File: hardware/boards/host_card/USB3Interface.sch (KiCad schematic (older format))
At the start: 8 parts, among them J2 USB3_Micro_B_Amphenol, J5 Conn_02x04_Odd_Even, U1 ECP5UM5G-381caBGA, U3 CYUSB3014, U6 128MiB

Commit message: Added a fiducial to for U7. Changed the two pin-headers to the keyd  samtec connectors. Some other misc updates
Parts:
- J5: footprint Connector_PinHeader_1.27mm:PinHeader_2x05_P1.27mm_Vertical -> lethalbit-connectors:FTSH-105-01-L-DV-K-TR
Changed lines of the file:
@@
 F 0 "J5" H 6400 7150 50  0000 C CNN
 F 1 "Conn_02x04_Odd_Even" H 6400 7250 50  0000 C CNN
-F 2 "Connector_PinHeader_1.27mm:PinHeader_2x05_P1.27mm_Vertical" H 6350 6800 50  0001 C CNN
+F 2 "lethalbit-connectors:FTSH-105-01-L-DV-K-TR" H 6350 6800 50  0001 C CNN
 F 3 "~" H 6350 6800 50  0001 C CNN
 	1    6350 6800

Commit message: Fixed up the consistancy of value naming, 100nF -> 0.1uF. Added the caps for the USB SSRX lines, moved the Ferrite for VBUS to fix a net naming issue
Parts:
- added C77, C78: 0.1uF, Capacitor_SMD:C_0402_1005Metric, symbol Device:C_Small
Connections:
- net SSTX+: now also C77.2; no longer U3.A5 (SSTX_P)
- net SSTX-: now also C78.2; no longer U3.A6 (SSTX_N)
- new net: C78.1, U3.A6 (SSTX_N)
- new net: C77.1, U3.A5 (SSTX_P)
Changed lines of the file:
@@
 	800  700  1050 700
 Wire Wire Line
-	2350 1800 3600 1800
-Wire Wire Line
 	3600 1800 3600 1550
 Wire Wire Line
 	3600 1550 3450 1550
 Wire Wire Line
-	2350 1900 3650 1900
-Wire Wire Line
 	3650 1900 3650 1650
 Wire Wire Line
 	3650 1650 3450 1650
 Wire Wire Line
-	2350 2050 3800 2050
+	2350 2050 3150 2050
 Wire Wire Line
 	3800 2050 3800 1250
@@
 	3800 1250 3450 1250
 Wire Wire Line
-	2350 2150 3850 2150
+	2350 2150 3050 2150
 Wire Wire Line
 	3850 2150 3850 1350
@@
 Text Notes 5900 3750 0    50   ~ 0
 PHY Boot config\n0 0 X - Sync ADMux\n1 0 X - Async ADMux\n1 1 X - USB\n1 X 0 - SPI, USB On failure
+Wire Wire Line
+	2350 1900 3650 1900
+Wire Wire Line
+	2350 1800 3600 1800
+$Comp
+L Device:C_Small C?
+U 1 1 5F3166F0
+P 3150 2150
+AR Path="/5EF66188/5F3166F0" Ref="C?"  Part="1"
+AR Path="/5ED4B101/5F3166F0" Ref="C?"  Part="1"
+AR Path="/5F2CAFD2/5F3166F0" Ref="C77"  Part="1"
+F 0 "C77" V 3200 1950 50  0000 L CNN
+F 1 "0.1uF" V 3350 2250 50  0000 L CNN
+F 2 "Capacitor_SMD:C_0402_1005Metric" H 3150 2150 50  0001 C CNN
+F 3 "~" H 3150 2150 50  0001 C CNN
+F 4 "KEMET" H 3150 2150 50  0001 C CNN "MFR"
+F 5 "C0402C104M8PACTU" H 3150 2150 50  0001 C CNN "MPN"
+	1    3150 2150
+	0    1    -1   0
+$EndComp
+$Comp
+L Device:C_Small C?
+U 1 1 5F3166E8
+P 3250 2050
+AR Path="/5EF66188/5F3166E8" Ref="C?"  Part="1"
+AR Path="/5ED4B101/5F3166E8" Ref="C?"  Part="1"
+AR Path="/5F2CAFD2/5F3166E8" Ref="C78"  Part="1"
+F 0 "C78" V 3300 1850 50  0000 L CNN
+F 1 "0.1uF" V 3350 2050 50  0000 L CNN
+F 2 "Capacitor_SMD:C_0402_1005Metric" H 3250 2050 50  0001 C CNN
+F 3 "~" H 3250 2050 50  0001 C CNN
+F 4 "KEMET" H 3250 2050 50  0001 C CNN "MFR"
+F 5 "C0402C104M8PACTU" H 3250 2050 50  0001 C CNN "MPN"
+	1    3250 2050
+	0    1    -1   0
+$EndComp
+Wire Wire Line
+	3250 2150 3850 2150
+Wire Wire Line
+	3350 2050 3800 2050
 Wire Bus Line
 	3150 3400 3150 4950

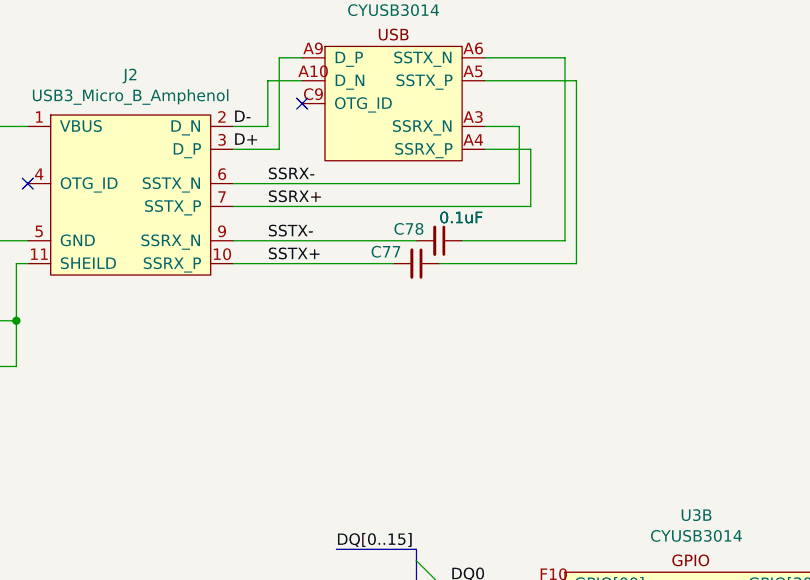
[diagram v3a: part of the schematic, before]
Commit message: Re-routed the USB side of things after adding the ESD diodes for the USB SS lines, still need to add the diode for the normal D+/D- pair
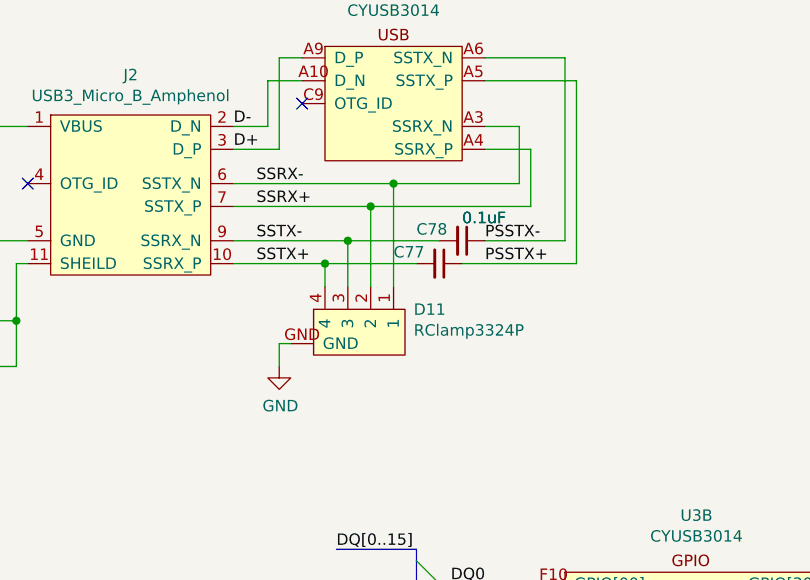
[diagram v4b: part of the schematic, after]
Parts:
- added D11: RClamp3324P, lethalbit:RClamp3324P, symbol lethalbit:RClamp3324P
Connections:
- net GND: now also D11.GND
- net SSRX+: now also D11.2
- net SSRX-: now also D11.1
- net SSTX+: now also D11.4
- net SSTX-: now also D11.3
- net PSSTX-: now reaches C78.1, U3.A6 (SSTX_N)
- net PSSTX+: now reaches C77.1, U3.A5 (SSTX_P)
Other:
- moved on the sheet: C77, C78
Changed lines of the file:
@@
 	3650 1650 3450 1650
 Wire Wire Line
-	2350 2050 3150 2050
+	2350 2050 2850 2050
 Wire Wire Line
 	3800 2050 3800 1250
@@
 	3800 1250 3450 1250
 Wire Wire Line
-	2350 2150 3050 2150
+	2350 2150 2750 2150
 Wire Wire Line
 	3850 2150 3850 1350
 Wire Wire Line
 	3850 1350 3450 1350
-Text Label 2500 1800 0    50   ~ 0
+Text Label 2450 1800 0    50   ~ 0
 SSRX-
-Text Label 2500 1900 0    50   ~ 0
+Text Label 2450 1900 0    50   ~ 0
 SSRX+
-Text Label 2500 2050 0    50   ~ 0
+Text Label 2450 2050 0    50   ~ 0
 SSTX-
-Text Label 2500 2150 0    50   ~ 0
+Text Label 2450 2150 0    50   ~ 0
 SSTX+
 Text Label 2350 1650 0    50   ~ 0
@@
 PHY Boot config\n0 0 X - Sync ADMux\n1 0 X - Async ADMux\n1 1 X - USB\n1 X 0 - SPI, USB On failure
 Wire Wire Line
-	2350 1900 3650 1900
-Wire Wire Line
-	2350 1800 3600 1800
+	2350 1900 2950 1900
+Wire Wire Line
+	2350 1800 3050 1800
 $Comp
 L Device:C_Small C?
 U 1 1 5F3166F0
-P 3150 2150
+P 3250 2150
 AR Path="/5EF66188/5F3166F0" Ref="C?"  Part="1"
 AR Path="/5ED4B101/5F3166F0" Ref="C?"  Part="1"
 AR Path="/5F2CAFD2/5F3166F0" Ref="C77"  Part="1"
-F 0 "C77" V 3200 1950 50  0000 L CNN
-F 1 "0.1uF" V 3350 2250 50  0000 L CNN
-F 2 "Capacitor_SMD:C_0402_1005Metric" H 3150 2150 50  0001 C CNN
-F 3 "~" H 3150 2150 50  0001 C CNN
-F 4 "KEMET" H 3150 2150 50  0001 C CNN "MFR"
-F 5 "C0402C104M8PACTU" H 3150 2150 50  0001 C CNN "MPN"
-	1    3150 2150
+F 0 "C77" V 3300 1950 50  0000 L CNN
+F 1 "0.1uF" V 3450 2250 50  0000 L CNN
+F 2 "Capacitor_SMD:C_0402_1005Metric" H 3250 2150 50  0001 C CNN
+F 3 "~" H 3250 2150 50  0001 C CNN
+F 4 "KEMET" H 3250 2150 50  0001 C CNN "MFR"
+F 5 "C0402C104M8PACTU" H 3250 2150 50  0001 C CNN "MPN"
+	1    3250 2150
 	0    1    -1   0
 $EndComp
@@
 L Device:C_Small C?
 U 1 1 5F3166E8
-P 3250 2050
+P 3350 2050
 AR Path="/5EF66188/5F3166E8" Ref="C?"  Part="1"
 AR Path="/5ED4B101/5F3166E8" Ref="C?"  Part="1"
 AR Path="/5F2CAFD2/5F3166E8" Ref="C78"  Part="1"
-F 0 "C78" V 3300 1850 50  0000 L CNN
-F 1 "0.1uF" V 3350 2050 50  0000 L CNN
-F 2 "Capacitor_SMD:C_0402_1005Metric" H 3250 2050 50  0001 C CNN
-F 3 "~" H 3250 2050 50  0001 C CNN
-F 4 "KEMET" H 3250 2050 50  0001 C CNN "MFR"
-F 5 "C0402C104M8PACTU" H 3250 2050 50  0001 C CNN "MPN"
-	1    3250 2050
+F 0 "C78" V 3400 1850 50  0000 L CNN
+F 1 "0.1uF" V 3450 2050 50  0000 L CNN
+F 2 "Capacitor_SMD:C_0402_1005Metric" H 3350 2050 50  0001 C CNN
+F 3 "~" H 3350 2050 50  0001 C CNN
+F 4 "KEMET" H 3350 2050 50  0001 C CNN "MFR"
+F 5 "C0402C104M8PACTU" H 3350 2050 50  0001 C CNN "MPN"
+	1    3350 2050
 	0    1    -1   0
 $EndComp
 Wire Wire Line
-	3250 2150 3850 2150
-Wire Wire Line
-	3350 2050 3800 2050
+	3350 2150 3850 2150
+Wire Wire Line
+	3450 2050 3800 2050
+Text Label 3450 2050 0    50   ~ 0
+PSSTX-
+Text Label 3450 2150 0    50   ~ 0
+PSSTX+
+$Comp
+L lethalbit:RClamp3324P D11
+U 1 1 5F4285A2
+P 2900 2500
+F 0 "D11" H 2662 2351 50  0000 R CNN
+F 1 "RClamp3324P" H 2662 2442 50  0000 R CNN
+F 2 "lethalbit:RClamp3324P" H 2900 2650 50  0001 C CNN
+F 3 "https://semtech.my.salesforce.com/sfc/p/#E0000000JelG/a/2R0000001NiZ/qbDz15IGGVdaTdo1LADFZxj6et0pDkRtmnKBn3k6s2M" H 2900 2650 50  0001 C CNN
+F 4 "Semtech Corporation" H 2900 2500 50  0001 C CNN "MFR"
+F 5 "RCLAMP3324P.TNT" H 2900 2500 50  0001 C CNN "MPN"
+	1    2900 2500
+	-1   0    0    1
+$EndComp
+Wire Wire Line
+	3050 2250 3050 1800
+Connection ~ 3050 1800
+Wire Wire Line
+	3050 1800 3600 1800
+Wire Wire Line
+	2950 2250 2950 1900
+Connection ~ 2950 1900
+Wire Wire Line
+	2950 1900 3650 1900
+Wire Wire Line
+	2850 2250 2850 2050
+Connection ~ 2850 2050
+Wire Wire Line
+	2850 2050 3250 2050
+Wire Wire Line
+	2750 2250 2750 2150
+Connection ~ 2750 2150
+Wire Wire Line
+	2750 2150 3150 2150
+$Comp
+L power:GND #PWR0144
+U 1 1 5F45C5E7
+P 2550 2600
+F 0 "#PWR0144" H 2550 2350 50  0001 C CNN
+F 1 "GND" H 2555 2427 50  0000 C CNN
+F 2 "" H 2550 2600 50  0001 C CNN
+F 3 "" H 2550 2600 50  0001 C CNN
+	1    2550 2600
+	1    0    0    -1
+$EndComp
+Wire Wire Line
+	2600 2500 2550 2500
+Wire Wire Line
+	2550 2500 2550 2600
 Wire Bus Line
 	3150 3400 3150 4950

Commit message: Roughly grouped unplaced parts together based on what they are related to
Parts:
- added D12: RClamp0512, lethalbit:RClamp0512, symbol lethalbit:RClamp0512
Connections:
- net D+: now also D12.2
- net D-: now also D12.1
- net GND: now also D12.GND
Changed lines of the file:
@@
 	2350 1550 2500 1550
 Wire Wire Line
-	2500 1550 2500 1350
+	2500 1550 2500 1400
 Wire Wire Line
 	2500 1350 2650 1350
@@
 Wire Wire Line
 	2550 2500 2550 2600
+$Comp
+L lethalbit:RClamp0512 D12
+U 1 1 5FB167E7
+P 2450 850
+F 0 "D12" H 2508 1125 50  0000 C CNN
+F 1 "RClamp0512" H 2508 1034 50  0000 C CNN
+F 2 "lethalbit:RClamp0512" H 2450 1000 50  0001 C CNN
+F 3 "https://media.digikey.com/pdf/Data%20Sheets/Semtech%20PDFs/RCLAMP0512TQ_Rev6_12-17-15.pdf" H 2450 1000 50  0001 C CNN
+F 4 "Sametech" H 2450 850 50  0001 C CNN "MFR"
+F 5 "RCLAMP0512TQTCT" H 2450 850 50  0001 C CNN "MPN"
+	1    2450 850
+	1    0    0    -1
+$EndComp
+Wire Wire Line
+	2350 1050 2350 1400
+Wire Wire Line
+	2350 1400 2500 1400
+Connection ~ 2500 1400
+Wire Wire Line
+	2500 1400 2500 1350
+Wire Wire Line
+	2550 1050 2550 1250
+Connection ~ 2550 1250
+$Comp
+L power:GND #PWR0147
+U 1 1 5FB26D21
+P 2750 900
+F 0 "#PWR0147" H 2750 650 50  0001 C CNN
+F 1 "GND" H 2755 727 50  0000 C CNN
+F 2 "" H 2750 900 50  0001 C CNN
+F 3 "" H 2750 900 50  0001 C CNN
+	1    2750 900
+	1    0    0    -1
+$EndComp
+Wire Wire Line
+	2750 800  2750 900
 Wire Bus Line
 	3150 3400 3150 4950

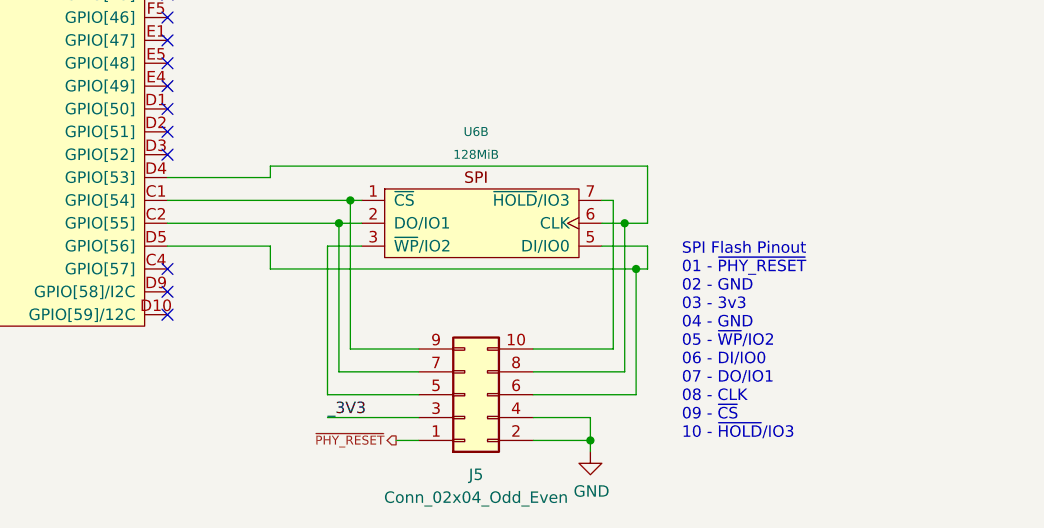
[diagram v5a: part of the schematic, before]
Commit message: Added a pin-header for the FPGA SPI flash lines to allow for the USB PHY to do a DFU update of the gateware when closed
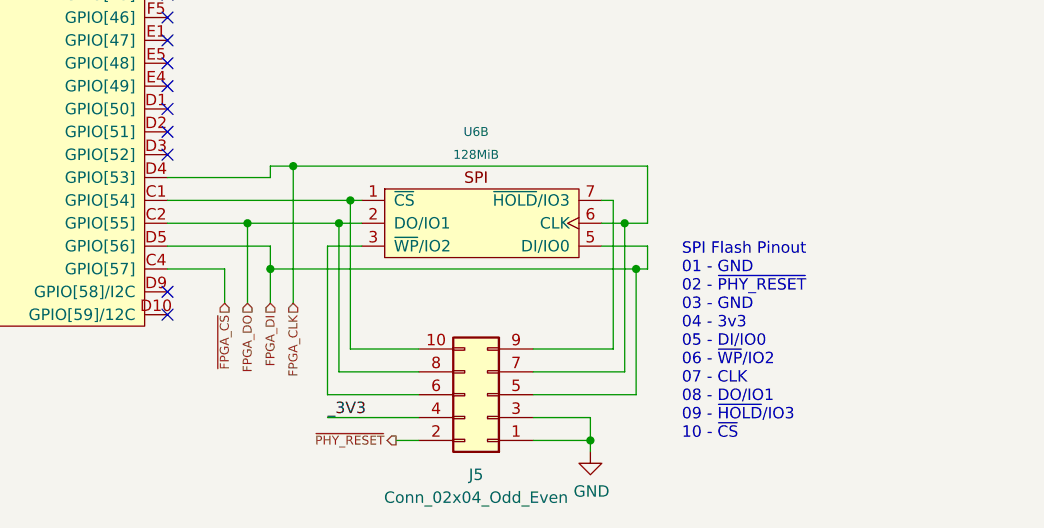
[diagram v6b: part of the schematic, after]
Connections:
- net 3V3: now also J5.4 (Pin_4); no longer J5.3 (Pin_3)
- net GND: now also J5.1 (Pin_1), J5.3 (Pin_3); no longer J5.2 (Pin_2), J5.4 (Pin_4)
- net ~PHY_RESET: now also J5.2 (Pin_2); no longer J5.1 (Pin_1)
- net at U3.C1 (GPIO[54]), U6.1 (~CS): now also J5.10 (Pin_10); no longer J5.9 (Pin_9)
- net FPGA_DO: now reaches U3.C2 (GPIO[55]), U6.2 (DO/IO1)
- net FPGA_DO: now also J5.8 (Pin_8); no longer J5.7 (Pin_7)
- net ~FPGA_CS: now reaches U3.C4 (GPIO[57])
- net FPGA_CLK: now reaches U3.D4 (GPIO[53]), U6.6 (CLK)
- net FPGA_CLK: now also J5.7 (Pin_7); no longer J5.8 (Pin_8)
- net FPGA_DI: now reaches U3.D5 (GPIO[56]), U6.5 (DI/IO0)
- net FPGA_DI: now also J5.5 (Pin_5); no longer J5.6 (Pin_6)
- net at U6.3 (~WP~/IO2): now also J5.6 (Pin_6); no longer J5.5 (Pin_5)
- net at U6.7 (~HOLD~/IO3): now also J5.9 (Pin_9); no longer J5.10 (Pin_10)
- no-connect marks 49 -> 48
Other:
- note added: "SPI Flash Pinout\n01 - GND\n02 - ~PHY_RESET~\n03 - GND\n04 - 3v3\n05 - DI/IO0\n06 - ~WP~/IO2\n07 - CLK\n08 - DO/IO1\n09 - ~HOLD~/IO3\n10 - ~CS~\n"
- note removed: "SPI Flash Pinout\n01 - ~PHY_RESET~\n02 - GND\n03 - 3v3\n04 - GND\n05 - ~WP~/IO2\n06 - DI/IO0\n07 - DO/IO1\n08 - CLK\n09 - ~CS~\n10 - ~HOLD~/IO3\n"
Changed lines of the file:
@@
 NoConn ~ 5050 6450
 NoConn ~ 5050 6350
-NoConn ~ 5050 6250
 NoConn ~ 5050 4150
 NoConn ~ 5050 4050
@@
 L Connector_Generic:Conn_02x05_Odd_Even J?
 U 1 1 60F06E66
-P 6350 6800
+P 6450 6800
 AR Path="/5EF66251/60F06E66" Ref="J?"  Part="1"
 AR Path="/5F2CAFD2/60F06E66" Ref="J5"  Part="1"
-F 0 "J5" H 6400 7150 50  0000 C CNN
-F 1 "Conn_02x04_Odd_Even" H 6400 7250 50  0000 C CNN
-F 2 "lethalbit-connectors:FTSH-105-01-L-DV-K-TR" H 6350 6800 50  0001 C CNN
-F 3 "~" H 6350 6800 50  0001 C CNN
-	1    6350 6800
-	1    0    0    1
+F 0 "J5" H 6500 7150 50  0000 C CNN
+F 1 "Conn_02x04_Odd_Even" H 6500 7250 50  0000 C CNN
+F 2 "lethalbit-connectors:FTSH-105-01-L-DV-K-TR" H 6450 6800 50  0001 C CNN
+F 3 "~" H 6450 6800 50  0001 C CNN
+	1    6450 6800
+	-1   0    0    1
 $EndComp
 $Comp
@@
 	7100 6250 5500 6250
 Wire Wire Line
-	6150 6600 5850 6600
-Wire Wire Line
 	5850 6600 5850 5950
 Connection ~ 5850 5950
@@
 Wire Wire Line
 	5800 6050 5800 6700
-Wire Wire Line
-	5800 6700 6150 6700
 Connection ~ 5800 6050
 Wire Wire Line
-	5800 6050 5050 6050
+	5800 6050 5400 6050
 Wire Wire Line
 	5900 6150 5750 6150
 Wire Wire Line
 	5750 6150 5750 6800
-Wire Wire Line
-	5750 6800 6150 6800
 Wire Wire Line
 	6050 7000 6150 7000
@@
 Wire Wire Line
 	6900 7000 6900 7050
-Wire Wire Line
-	6150 6900 5750 6900
 Text Label 5750 6900 0    50   ~ 0
 _3V3
@@
 _3V3
 Text Notes 7300 7000 0    50   ~ 0
-SPI Flash Pinout\n01 - ~PHY_RESET~\n02 - GND\n03 - 3v3\n04 - GND\n05 - ~WP~/IO2\n06 - DI/IO0\n07 - DO/IO1\n08 - CLK\n09 - ~CS~\n10 - ~HOLD~/IO3\n
+SPI Flash Pinout\n01 - GND\n02 - ~PHY_RESET~\n03 - GND\n04 - 3v3\n05 - DI/IO0\n06 - ~WP~/IO2\n07 - CLK\n08 - DO/IO1\n09 - ~HOLD~/IO3\n10 - ~CS~\n
 Entry Wire Line
 	9000 3550 9100 3650
@@
 	5500 5850 5050 5850
 Wire Wire Line
-	5500 5800 7150 5800
+	5500 5800 5600 5800
 Wire Wire Line
 	7150 5800 7150 6050
@@
 Wire Wire Line
 	2750 800  2750 900
+Wire Wire Line
+	5750 6900 6150 6900
+Wire Wire Line
+	5750 6800 6150 6800
+Wire Wire Line
+	5800 6700 6150 6700
+Wire Wire Line
+	5850 6600 6150 6600
+Text HLabel 5300 6400 3    39   Input ~ 0
+~FPGA_CS
+Text HLabel 5400 6400 3    39   Input ~ 0
+FPGA_DO
+Text HLabel 5500 6400 3    39   Input ~ 0
+FPGA_DI
+Text HLabel 5600 6400 3    39   Input ~ 0
+FPGA_CLK
+Wire Wire Line
+	5500 6250 5500 6400
+Connection ~ 5500 6250
+Wire Wire Line
+	5400 6050 5400 6400
+Connection ~ 5400 6050
+Wire Wire Line
+	5400 6050 5050 6050
+Wire Wire Line
+	5600 5800 5600 6400
+Connection ~ 5600 5800
+Wire Wire Line
+	5600 5800 7150 5800
+Wire Wire Line
+	5050 6250 5300 6250
+Wire Wire Line
+	5300 6250 5300 6400
 Wire Bus Line
 	3150 3400 3150 4950

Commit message: Started poking the SPI flash for the USB PHY
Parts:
- R59: footprint Resistor_SMD:R_0603_1608Metric -> Resistor_SMD:R_0402_1005Metric; MPN CRCW06031K00FKEAHP -> RCS04021K00FKED
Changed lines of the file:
@@
 F 0 "R59" H 5709 3446 50  0000 L CNN
 F 1 "1k" H 5709 3355 50  0000 L CNN
-F 2 "Resistor_SMD:R_0603_1608Metric" H 5650 3400 50  0001 C CNN
+F 2 "Resistor_SMD:R_0402_1005Metric" H 5650 3400 50  0001 C CNN
 F 3 "~" H 5650 3400 50  0001 C CNN
 F 4 "Vishay Dale" H 5650 3400 50  0001 C CNN "MFR"
-F 5 "CRCW06031K00FKEAHP" H 5650 3400 50  0001 C CNN "MPN"
+F 5 "RCS04021K00FKED" H 5650 3400 50  0001 C CNN "MPN"
 	1    5650 3400
 	1    0    0    -1
